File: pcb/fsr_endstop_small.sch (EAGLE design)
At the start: 30 parts, among them U1 ATTINY461

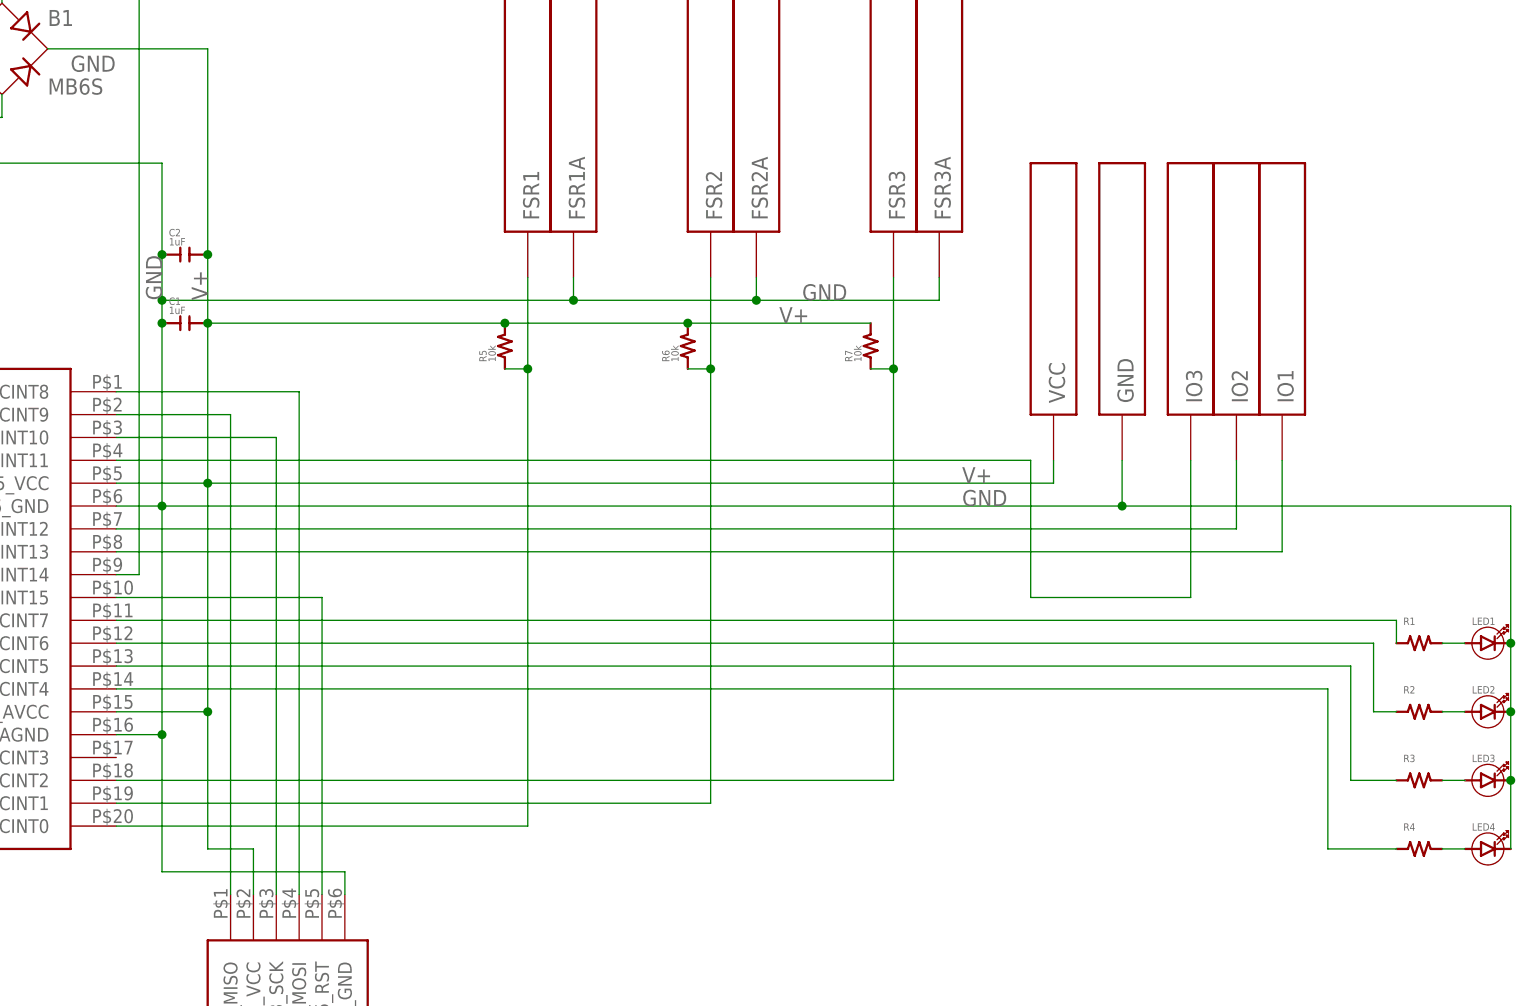
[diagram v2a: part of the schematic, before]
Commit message: Revision 1.2 includes three jumpers for modifying settings.
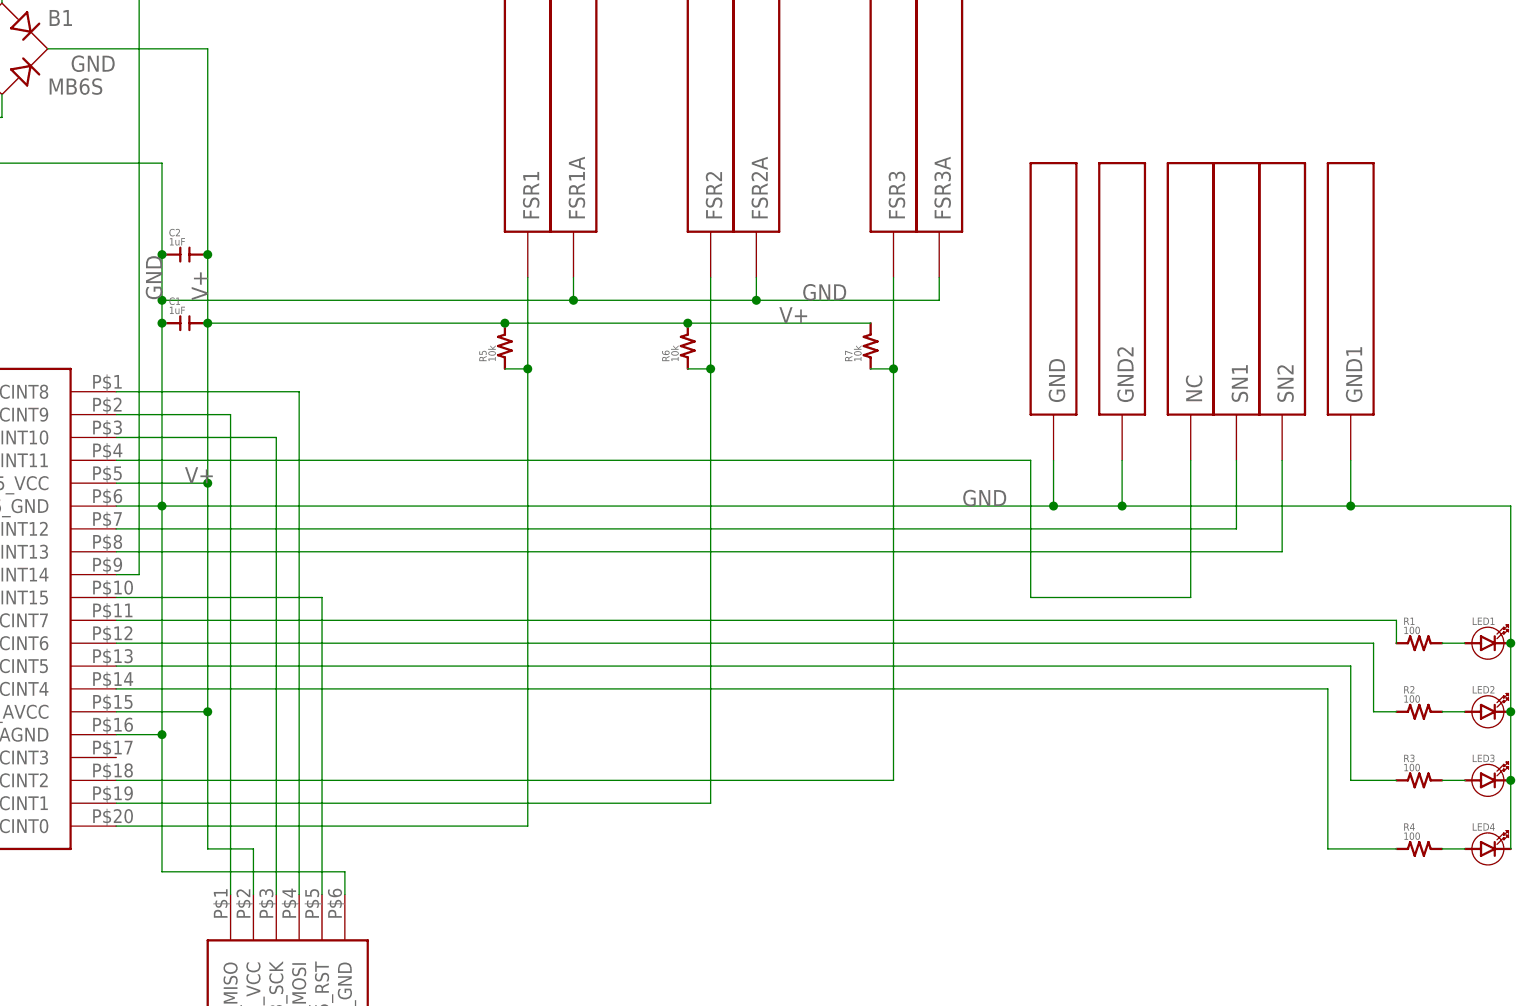
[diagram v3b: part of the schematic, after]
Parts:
- removed VCC: PIN1.2MM, _sg_lib:PIN1.2MM
- added GND1, GND2: PIN1.2MM, _sg_lib:PIN1.2MM
- R1, R2, R3, R4: value (none) -> 100
- renumbered IO1 to SN2, IO2 to SN1, IO3 to NC
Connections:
- net GND: now also GND1.P$1, GND2.P$1
- net V+: no longer VCC.P$1
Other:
- moved on the sheet: GND
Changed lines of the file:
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@@
 <part name="LED3" library="_sg_lib" deviceset="LED0603" device=""/>
 <part name="LED4" library="_sg_lib" deviceset="LED0603" device=""/>
-<part name="R1" library="_sg_lib" deviceset="RES0603" device=""/>
-<part name="R2" library="_sg_lib" deviceset="RES0603" device=""/>
-<part name="R3" library="_sg_lib" deviceset="RES0603" device=""/>
-<part name="R4" library="_sg_lib" deviceset="RES0603" device=""/>
+<part name="R1" library="_sg_lib" deviceset="RES0603" device="" value="100"/>
+<part name="R2" library="_sg_lib" deviceset="RES0603" device="" value="100"/>
+<part name="R3" library="_sg_lib" deviceset="RES0603" device="" value="100"/>
+<part name="R4" library="_sg_lib" deviceset="RES0603" device="" value="100"/>
 <part name="R5" library="_sg_lib" deviceset="RES0603" device="" value="10k"/>
 <part name="R6" library="_sg_lib" deviceset="RES0603" device="" value="10k"/>
 <part name="R7" library="_sg_lib" deviceset="RES0603" device="" value="10k"/>
-<part name="IO1" library="_sg_lib" deviceset="PIN" device="1.2MM"/>
-<part name="IO2" library="_sg_lib" deviceset="PIN" device="1.2MM"/>
-<part name="IO3" library="_sg_lib" deviceset="PIN" device="1.2MM"/>
+<part name="SN2" library="_sg_lib" deviceset="PIN" device="1.2MM"/>
+<part name="SN1" library="_sg_lib" deviceset="PIN" device="1.2MM"/>
+<part name="NC" library="_sg_lib" deviceset="PIN" device="1.2MM"/>
+<part name="GND2" library="_sg_lib" deviceset="PIN" device="1.2MM"/>
 <part name="GND" library="_sg_lib" deviceset="PIN" device="1.2MM"/>
-<part name="VCC" library="_sg_lib" deviceset="PIN" device="1.2MM"/>
 <part name="C2" library="_sg_lib" deviceset="CAP0603" device="" value="1uF"/>
 <part name="B1" library="rectifier" deviceset="MB*S" device="" technology="6"/>
+<part name="GND1" library="_sg_lib" deviceset="PIN" device="1.2MM"/>
 </parts>
 <sheets>
@@
 <instance part="R6" gate="G$1" x="101.6" y="76.2" rot="R90"/>
 <instance part="R7" gate="G$1" x="121.92" y="76.2" rot="R90"/>
-<instance part="IO1" gate="G$1" x="167.64" y="68.58" rot="R270"/>
-<instance part="IO2" gate="G$1" x="162.56" y="68.58" rot="R270"/>
-<instance part="IO3" gate="G$1" x="157.48" y="68.58" rot="R270"/>
-<instance part="GND" gate="G$1" x="149.86" y="68.58" rot="R270"/>
-<instance part="VCC" gate="G$1" x="142.24" y="68.58" rot="R270"/>
+<instance part="SN2" gate="G$1" x="167.64" y="68.58" rot="R270"/>
+<instance part="SN1" gate="G$1" x="162.56" y="68.58" rot="R270"/>
+<instance part="NC" gate="G$1" x="157.48" y="68.58" rot="R270"/>
+<instance part="GND2" gate="G$1" x="149.86" y="68.58" rot="R270"/>
+<instance part="GND" gate="G$1" x="142.24" y="68.58" rot="R270"/>
 <instance part="C2" gate="G$1" x="45.72" y="86.36"/>
 <instance part="B1" gate="G$1" x="25.4" y="109.22"/>
+<instance part="GND1" gate="G$1" x="175.26" y="68.58" rot="R270"/>
 </instances>
 <busses>
@@
 <pinref part="R7" gate="G$1" pin="P$2"/>
 <label x="111.76" y="78.74" size="1.778" layer="95"/>
-<pinref part="VCC" gate="G$1" pin="P$1"/>
-<wire x1="48.26" y1="60.96" x2="142.24" y2="60.96" width="0.1524" layer="91"/>
-<wire x1="142.24" y1="60.96" x2="142.24" y2="63.5" width="0.1524" layer="91"/>
-<label x="132.08" y="60.96" size="1.778" layer="95"/>
+<label x="45.72" y="60.96" size="1.778" layer="95"/>
 <pinref part="C2" gate="G$1" pin="P$2"/>
 <junction x="48.26" y="86.36"/>
@@
 <junction x="88.9" y="81.28"/>
 <label x="114.3" y="81.28" size="1.778" layer="95"/>
-<pinref part="GND" gate="G$1" pin="P$1"/>
-<wire x1="43.18" y1="58.42" x2="149.86" y2="58.42" width="0.1524" layer="91"/>
+<pinref part="GND2" gate="G$1" pin="P$1"/>
+<wire x1="43.18" y1="58.42" x2="142.24" y2="58.42" width="0.1524" layer="91"/>
+<wire x1="142.24" y1="58.42" x2="149.86" y2="58.42" width="0.1524" layer="91"/>
 <wire x1="149.86" y1="58.42" x2="149.86" y2="63.5" width="0.1524" layer="91"/>
 <label x="132.08" y="58.42" size="1.778" layer="95"/>
-<wire x1="149.86" y1="58.42" x2="193.04" y2="58.42" width="0.1524" layer="91"/>
+<wire x1="149.86" y1="58.42" x2="175.26" y2="58.42" width="0.1524" layer="91"/>
+<wire x1="175.26" y1="58.42" x2="193.04" y2="58.42" width="0.1524" layer="91"/>
 <wire x1="193.04" y1="58.42" x2="193.04" y2="43.18" width="0.1524" layer="91"/>
 <junction x="149.86" y="58.42"/>
@@
 <pinref part="B1" gate="G$1" pin="-"/>
 <wire x1="17.78" y1="109.22" x2="20.32" y2="109.22" width="0.1524" layer="91"/>
+<pinref part="GND" gate="G$1" pin="P$1"/>
+<wire x1="142.24" y1="63.5" x2="142.24" y2="58.42" width="0.1524" layer="91"/>
+<junction x="142.24" y="58.42"/>
+<pinref part="GND1" gate="G$1" pin="P$1"/>
+<wire x1="175.26" y1="63.5" x2="175.26" y2="58.42" width="0.1524" layer="91"/>
+<junction x="175.26" y="58.42"/>
 </segment>
 </net>
@@
 <pinref part="U1" gate="G$1" pin="8_PB5_ADC6/OC1D/CLK0/XTAL2/PCINT13"/>
 <wire x1="38.1" y1="53.34" x2="167.64" y2="53.34" width="0.1524" layer="91"/>
-<pinref part="IO1" gate="G$1" pin="P$1"/>
+<pinref part="SN2" gate="G$1" pin="P$1"/>
 <wire x1="167.64" y1="53.34" x2="167.64" y2="63.5" width="0.1524" layer="91"/>
 </segment>
@@
 <pinref part="U1" gate="G$1" pin="7_PB4_ADC7/OC1D#/CLKI/XTAL1/PCINT12"/>
 <wire x1="38.1" y1="55.88" x2="162.56" y2="55.88" width="0.1524" layer="91"/>
-<pinref part="IO2" gate="G$1" pin="P$1"/>
+<pinref part="SN1" gate="G$1" pin="P$1"/>
 <wire x1="162.56" y1="55.88" x2="162.56" y2="63.5" width="0.1524" layer="91"/>
 </segment>
@@
 <wire x1="38.1" y1="63.5" x2="139.7" y2="63.5" width="0.1524" layer="91"/>
 <wire x1="139.7" y1="63.5" x2="139.7" y2="48.26" width="0.1524" layer="91"/>
-<pinref part="IO3" gate="G$1" pin="P$1"/>
+<pinref part="NC" gate="G$1" pin="P$1"/>
 <wire x1="139.7" y1="48.26" x2="157.48" y2="48.26" width="0.1524" layer="91"/>
 <wire x1="157.48" y1="48.26" x2="157.48" y2="63.5" width="0.1524" layer="91"/>
@@
 </sheet>
 </sheets>
+<errors>
+</errors>
 </schematic>
 </drawing>
